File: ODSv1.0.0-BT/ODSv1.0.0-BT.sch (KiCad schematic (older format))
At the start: 0 parts

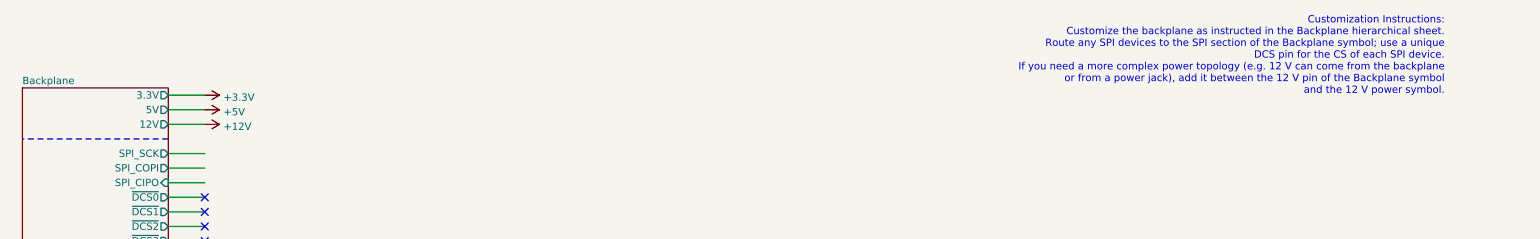
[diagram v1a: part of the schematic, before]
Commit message: Remap pins for easier layout
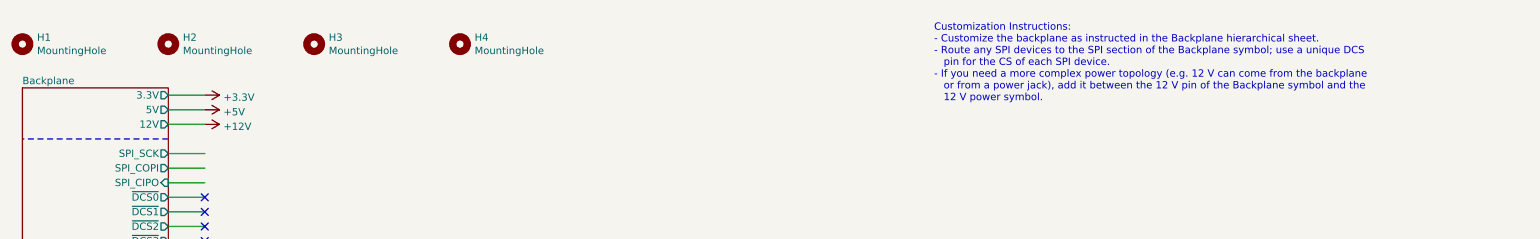
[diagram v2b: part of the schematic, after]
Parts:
- added H1, H2, H3, H4: MountingHole, MountingHole:MountingHole_3.2mm_M3, symbol Mechanical:MountingHole
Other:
- note added: "Customization Instructions:\n- Customize the backplane as instructed in the Backplane hierarchical sheet.\n- Route any SPI devices to the SPI section of the Backplane symbol; use a unique DCS\n pin for the CS of each SPI device.\n- If you need a more complex power topology (e.g. 12 V can come from the backplane\n or from a power jack), add it between the 12 V pin of the Backplane symbol and the\n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"
- note removed: "Customization Instructions:\nCustomize the backplane as instructed in the Backplane hierarchical sheet.\nRoute any SPI devices to the SPI section of the Backplane symbol; use a unique\nDCS pin for the CS of each SPI device.\nIf you need a more complex power topology (e.g. 12 V can come from the backplane\nor from a power jack), add it between the 12 V pin of the Backplane symbol\nand the 12 V pow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"
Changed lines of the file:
@@
 	750  3350 1750 3350
 $Comp
-L power:+3.3V #PWR0101
+L power:+3.3V #PWR01
 U 1 1 628D4BB4
 P 2000 1050
-F 0 "#PWR0101" H 2000 900 50  0001 C CNN
+F 0 "#PWR01" H 2000 900 50  0001 C CNN
 F 1 "+3.3V" V 2015 1178 50  0000 L CNN
 F 2 "" H 2000 1050 50  0001 C CNN
@@
 $EndComp
 $Comp
-L power:+5V #PWR0102
+L power:+5V #PWR02
 U 1 1 628D514B
 P 2000 1150
-F 0 "#PWR0102" H 2000 1000 50  0001 C CNN
+F 0 "#PWR02" H 2000 1000 50  0001 C CNN
 F 1 "+5V" V 2015 1278 50  0000 L CNN
 F 2 "" H 2000 1150 50  0001 C CNN
@@
 $EndComp
 $Comp
-L power:+12V #PWR0103
+L power:+12V #PWR03
 U 1 1 628D5574
 P 2000 1250
-F 0 "#PWR0103" H 2000 1100 50  0001 C CNN
+F 0 "#PWR03" H 2000 1100 50  0001 C CNN
 F 1 "+12V" V 2015 1378 50  0000 L CNN
 F 2 "" H 2000 1250 50  0001 C CNN
@@
 	0    1    1    0
 $EndComp
-Text Notes 10500 1050 2    50   ~ 0
-Customization Instructions:\nCustomize the backplane as instructed in the Backplane hierarchical sheet.\nRoute any SPI devices to the SPI section of the Backplane symbol; use a unique\nDCS pin for the CS of each SPI device.\nIf you need a more complex power topology (e.g. 12 V can come from the backplane\nor from a power jack), add it between the 12 V pin of the Backplane symbol\nand the 12 V power symbol.
+Text Notes 7000 1100 0    50   ~ 0
+Customization Instructions:\n- Customize the backplane as instructed in the Backplane hierarchical sheet.\n- Route any SPI devices to the SPI section of the Backplane symbol; use a unique DCS\n   pin for the CS of each SPI device.\n- If you need a more complex power topology (e.g. 12 V can come from the backplane\n   or from a power jack), add it between the 12 V pin of the Backplane symbol and the\n   12 V power symbol.
+$Comp
+L Mechanical:MountingHole H1
+U 1 1 600692B9
+P 750 700
+F 0 "H1" H 850 746 50  0000 L CNN
+F 1 "MountingHole" H 850 655 50  0000 L CNN
+F 2 "MountingHole:MountingHole_3.2mm_M3" H 750 700 50  0001 C CNN
+F 3 "~" H 750 700 50  0001 C CNN
+	1    750  700
+	1    0    0    -1
+$EndComp
+$Comp
+L Mechanical:MountingHole H2
+U 1 1 6006AFC8
+P 1750 700
+F 0 "H2" H 1850 746 50  0000 L CNN
+F 1 "MountingHole" H 1850 655 50  0000 L CNN
+F 2 "MountingHole:MountingHole_3.2mm_M3" H 1750 700 50  0001 C CNN
+F 3 "~" H 1750 700 50  0001 C CNN
+	1    1750 700
+	1    0    0    -1
+$EndComp
+$Comp
+L Mechanical:MountingHole H3
+U 1 1 6006B051
+P 2750 700
+F 0 "H3" H 2850 746 50  0000 L CNN
+F 1 "MountingHole" H 2850 655 50  0000 L CNN
+F 2 "MountingHole:MountingHole_3.2mm_M3" H 2750 700 50  0001 C CNN
+F 3 "~" H 2750 700 50  0001 C CNN
+	1    2750 700
+	1    0    0    -1
+$EndComp
+$Comp
+L Mechanical:MountingHole H4
+U 1 1 6006B0C5
+P 3750 700
+F 0 "H4" H 3850 746 50  0000 L CNN
+F 1 "MountingHole" H 3850 655 50  0000 L CNN
+F 2 "MountingHole:MountingHole_3.2mm_M3" H 3750 700 50  0001 C CNN
+F 3 "~" H 3750 700 50  0001 C CNN
+	1    3750 700
+	1    0    0    -1
+$EndComp
 $EndSCHEMATC

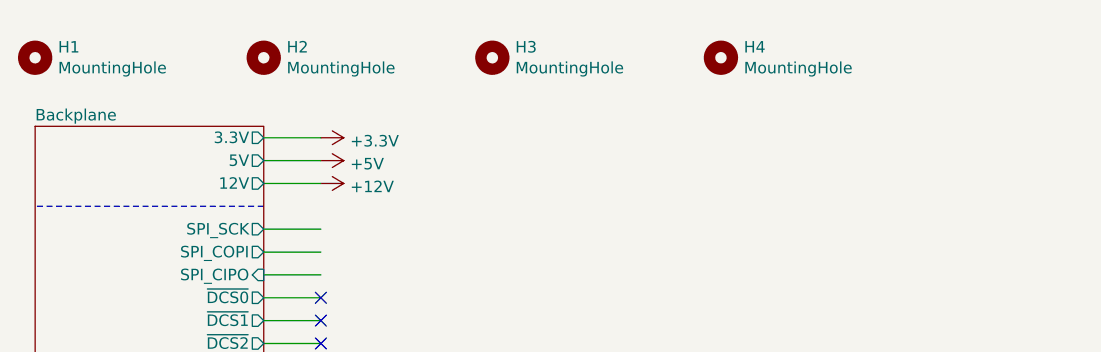
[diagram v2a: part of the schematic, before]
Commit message: Add silkscreen documentation text
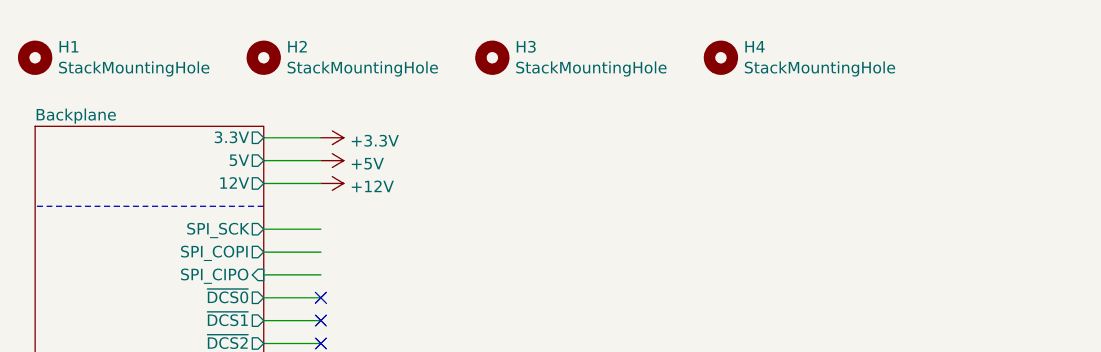
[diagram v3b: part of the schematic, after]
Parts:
- H1, H2, H3, H4: value MountingHole -> StackMountingHole
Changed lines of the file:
@@
 P 750 700
 F 0 "H1" H 850 746 50  0000 L CNN
-F 1 "MountingHole" H 850 655 50  0000 L CNN
+F 1 "StackMountingHole" H 850 655 50  0000 L CNN
 F 2 "MountingHole:MountingHole_3.2mm_M3" H 750 700 50  0001 C CNN
 F 3 "~" H 750 700 50  0001 C CNN
@@
 P 1750 700
 F 0 "H2" H 1850 746 50  0000 L CNN
-F 1 "MountingHole" H 1850 655 50  0000 L CNN
+F 1 "StackMountingHole" H 1850 655 50  0000 L CNN
 F 2 "MountingHole:MountingHole_3.2mm_M3" H 1750 700 50  0001 C CNN
 F 3 "~" H 1750 700 50  0001 C CNN
@@
 P 2750 700
 F 0 "H3" H 2850 746 50  0000 L CNN
-F 1 "MountingHole" H 2850 655 50  0000 L CNN
+F 1 "StackMountingHole" H 2850 655 50  0000 L CNN
 F 2 "MountingHole:MountingHole_3.2mm_M3" H 2750 700 50  0001 C CNN
 F 3 "~" H 2750 700 50  0001 C CNN
@@
 P 3750 700
 F 0 "H4" H 3850 746 50  0000 L CNN
-F 1 "MountingHole" H 3850 655 50  0000 L CNN
+F 1 "StackMountingHole" H 3850 655 50  0000 L CNN
 F 2 "MountingHole:MountingHole_3.2mm_M3" H 3750 700 50  0001 C CNN
 F 3 "~" H 3750 700 50  0001 C CNN

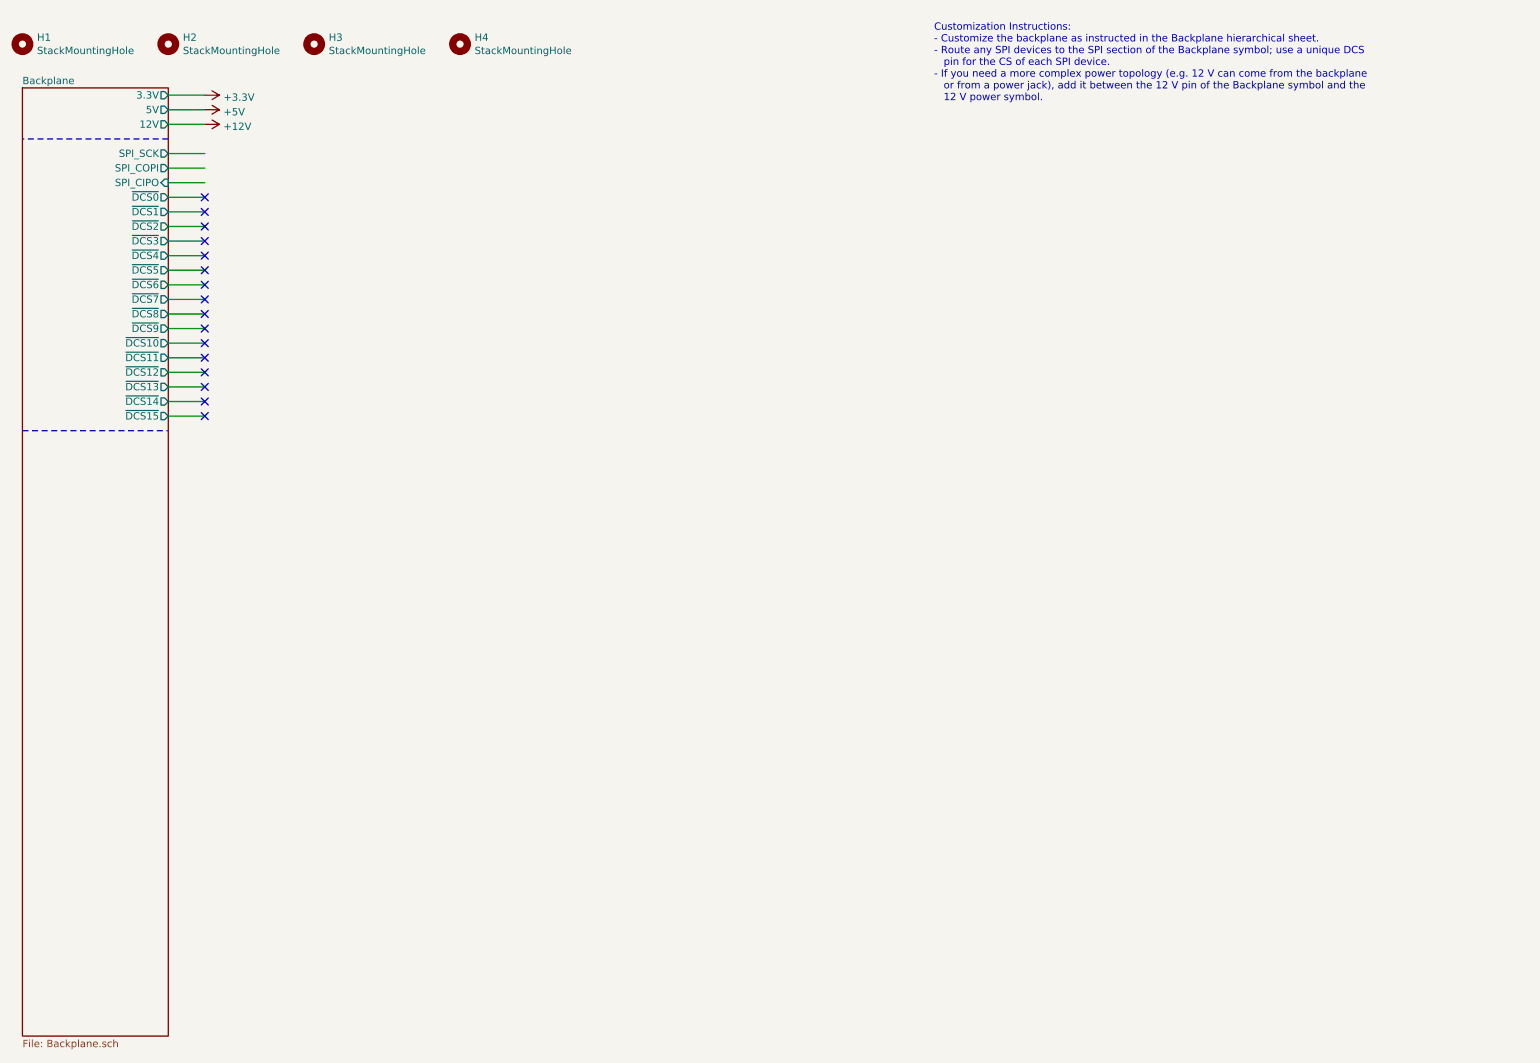
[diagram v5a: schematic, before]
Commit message: Add LICENSE files and README text, and rename backplane to backbone
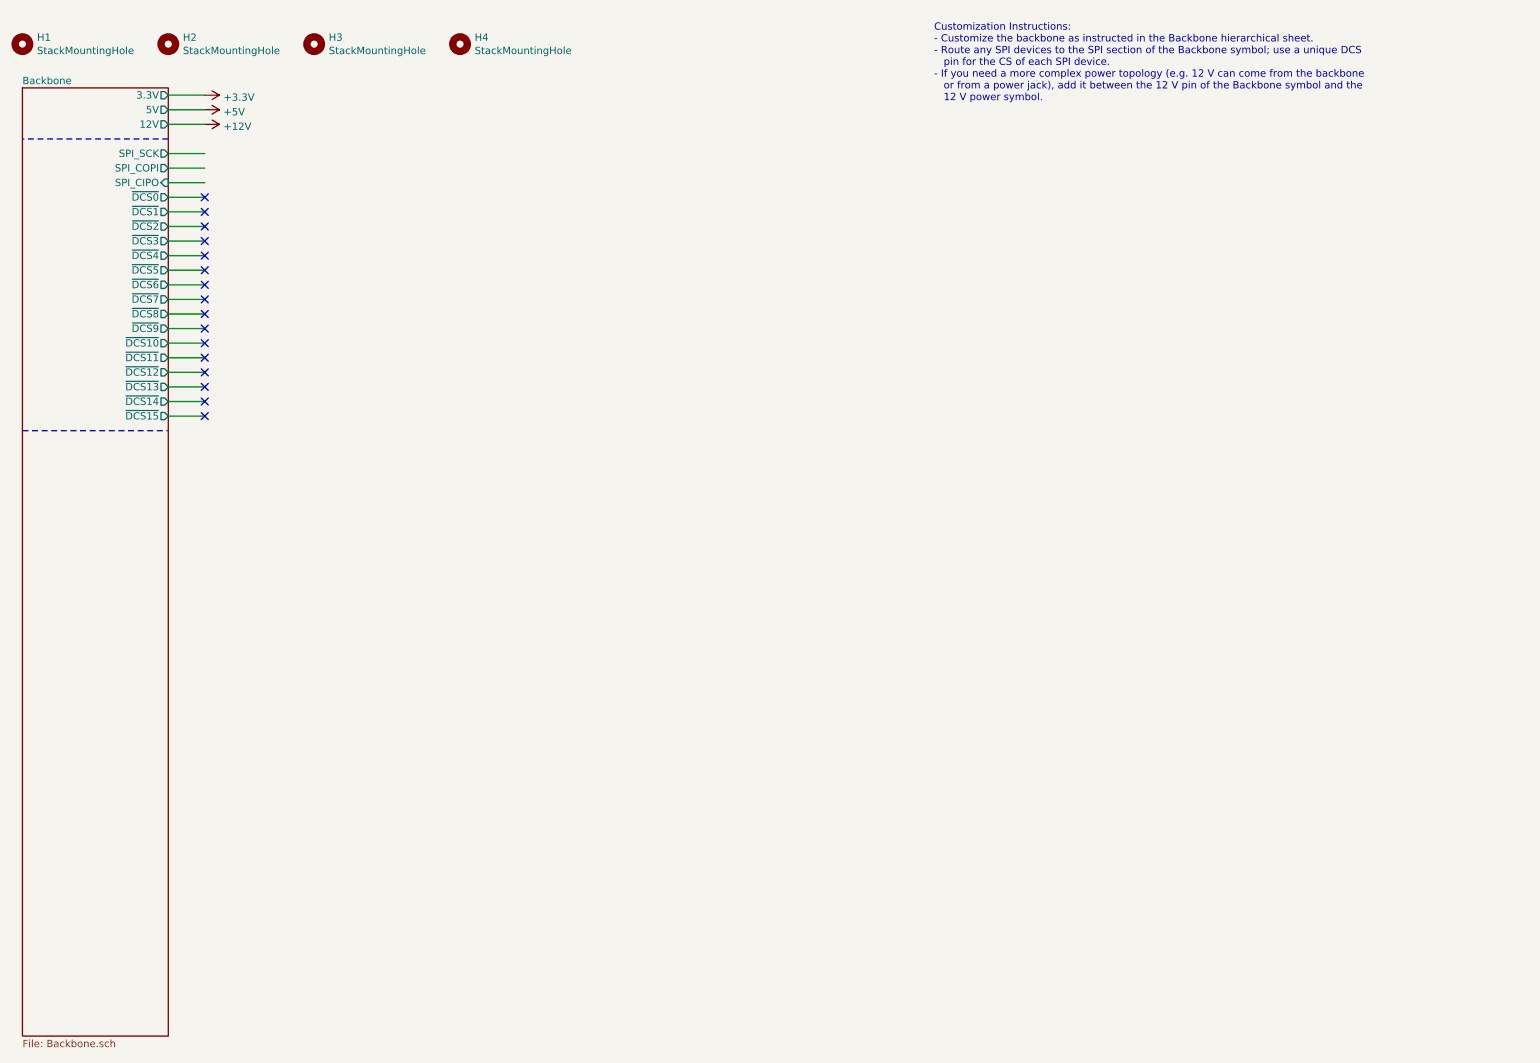
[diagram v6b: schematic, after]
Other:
- note added: "Customization Instructions:\n- Customize the backbone as instructed in the Backbone hierarchical sheet.\n- Route any SPI devices to the SPI section of the Backbone symbol; use a unique DCS\n pin for the CS of each SPI device.\n- If you need a more complex power topology (e.g. 12 V can come from the backbone\n or from a power jack), add it between the 12 V pin of the Backbone symbol and the\n 12 V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"
- note removed: "Customization Instructions:\n- Customize the backplane as instructed in the Backplane hierarchical sheet.\n- Route any SPI devices to the SPI section of the Backplane symbol; use a unique DCS\n pin for the CS of each SPI device.\n- If you need a more complex power topology (e.g. 12 V can come from the backplane\n or from a power jack), add it between the 12 V pin of the Backplane symbol and the\n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"
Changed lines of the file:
@@
 encoding utf-8
 Sheet 1 4
-Title "Backplane Template"
-Date "2020-12-31"
+Title "Backbone Template"
+Date "2021-01-19"
 Rev "v0.1.0"
 Comp "Prakash Lab/Octopi Team"
@@
 S 750  1000 1000 6500
 U 60C51399
-F0 "Backplane" 50
-F1 "Backplane.sch" 50
+F0 "Backbone" 50
+F1 "Backbone.sch" 50
 F2 "SPI_SCK" O R 1750 1450 50
 F3 "SPI_COPI" O R 1750 1550 50
@@
 $EndComp
 Text Notes 7000 1100 0    50   ~ 0
-Customization Instructions:\n- Customize the backplane as instructed in the Backplane hierarchical sheet.\n- Route any SPI devices to the SPI section of the Backplane symbol; use a unique DCS\n   pin for the CS of each SPI device.\n- If you need a more complex power topology (e.g. 12 V can come from the backplane\n   or from a power jack), add it between the 12 V pin of the Backplane symbol and the\n   12 V power symbol.
+Customization Instructions:\n- Customize the backbone as instructed in the Backbone hierarchical sheet.\n- Route any SPI devices to the SPI section of the Backbone symbol; use a unique DCS\n   pin for the CS of each SPI device.\n- If you need a more complex power topology (e.g. 12 V can come from the backbone\n   or from a power jack), add it between the 12 V pin of the Backbone symbol and the\n   12 V power symbol.
 $Comp
 L Mechanical:MountingHole H1
